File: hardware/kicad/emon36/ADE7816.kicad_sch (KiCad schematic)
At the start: 43 parts, among them J15 6_port_3.5mm_audio_jack_array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, J16 6_port_3.5mm_audio_jack_array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, U10 ADE7816

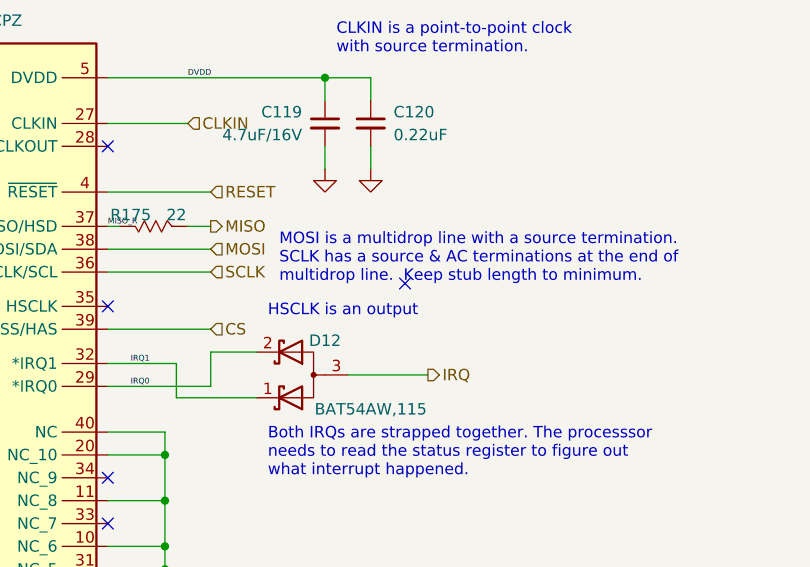
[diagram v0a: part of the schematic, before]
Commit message: Added diodes on IRQ, included solder mask and silk constraints, fix silk. Version sent to production.
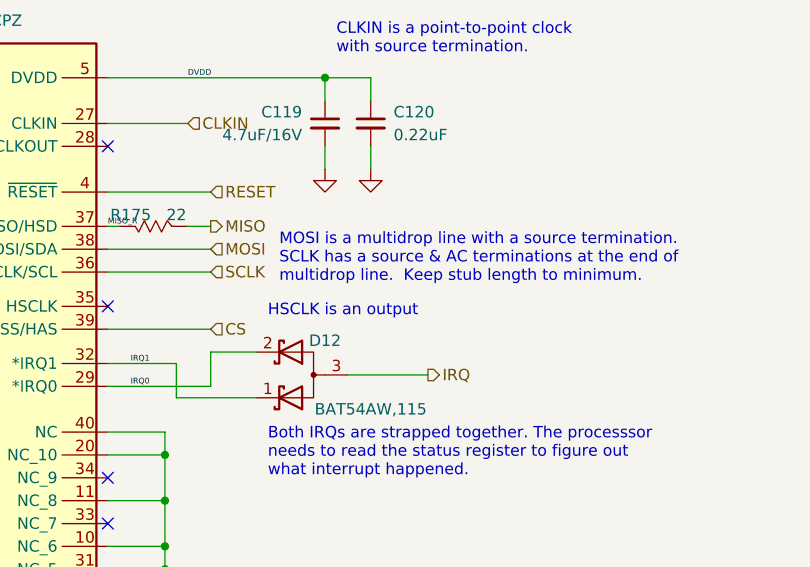
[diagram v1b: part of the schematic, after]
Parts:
- C107, C108, C109, C110, C111, C112, C117, C118: Desc (none) -> CAP CER 0.022UF 25V X7R 0603; MFR (none) -> Samsung Electro-Mechanics; MPN (none) -> CL10B222KB8NFNC
- C115, C120: Desc (none) -> CAP CER 0.22UF 25V X7R 0603; MFR (none) -> Samsung Electro-Mechanics; MPN (none) -> CL10B224KA8NNNC
- C116: Desc (none) -> CAP CER 0.1UF 50V X7R 0603; MFR (none) -> KYOCERA AVX; MPN (none) -> 06035C104KAT2A
- D12: Desc (none) -> DIODE ARRAY SCHOTTKY 30V SOT323
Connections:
- no-connect marks 19 -> 18
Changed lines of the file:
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@@
   (no_connect (at 46.99 53.34))
   (no_connect (at 195.58 62.23))
-  (no_connect (at 228.6 77.47))
   (no_connect (at 195.58 80.01))
   (wire (pts (xy 160.02 68.58) (xy 148.59 68.58))
@@
       (effects (font (size 1.27 1.27)) hide)
     )
+    (property "Desc" "CAP CER 0.022UF 25V X7R 0603" (id 4) (at 85.09 106.68 0)
+      (effects (font (size 1.27 1.27)) hide)
+    )
+    (property "MFR" "Samsung Electro-Mechanics" (id 5) (at 85.09 106.68 0)
+      (effects (font (size 1.27 1.27)) hide)
+    )
+    (property "MPN" "CL10B222KB8NFNC" (id 6) (at 85.09 106.68 0)
+      (effects (font (size 1.27 1.27)) hide)
+    )
     (pin "1")
     (pin "2")
@@
       (effects (font (size 1.27 1.27)) hide)
     )
+    (property "Desc" "CAP CER 0.022UF 25V X7R 0603" (id 4) (at 85.09 54.61 0)
+      (effects (font (size 1.27 1.27)) hide)
+    )
+    (property "MFR" "Samsung Electro-Mechanics" (id 5) (at 85.09 54.61 0)
+      (effects (font (size 1.27 1.27)) hide)
+    )
+    (property "MPN" "CL10B222KB8NFNC" (id 6) (at 85.09 54.61 0)
+      (effects (font (size 1.27 1.27)) hide)
+    )
     (pin "1")
     (pin "2")
@@
     )
     (property "MPN" "BAT54AW,115" (id 5) (at 224.79 91.44 0))
+    (property "Desc" "DIODE ARRAY SCHOTTKY 30V SOT323" (id 6) (at 217.17 87.63 0)
+      (effects (font (size 1.27 1.27)) hide)
+    )
     (pin "1")
     (pin "2")
@@
     )
     (property "Datasheet" "~" (id 3) (at 143.51 78.74 0)
+      (effects (font (size 1.27 1.27)) hide)
+    )
+    (property "Desc" "CAP CER 0.1UF 50V X7R 0603" (id 4) (at 143.51 78.74 0)
+      (effects (font (size 1.27 1.27)) hide)
+    )
+    (property "MFR" "KYOCERA AVX" (id 5) (at 143.51 78.74 0)
+      (effects (font (size 1.27 1.27)) hide)
+    )
+    (property "MPN" "06035C104KAT2A" (id 6) (at 143.51 78.74 0)
       (effects (font (size 1.27 1.27)) hide)
     )
@@
       (effects (font (size 1.27 1.27)) hide)
     )
+    (property "Desc" "CAP CER 0.22UF 25V X7R 0603" (id 4) (at 143.51 63.5 0)
+      (effects (font (size 1.27 1.27)) hide)
+    )
+    (property "MFR" "Samsung Electro-Mechanics" (id 5) (at 143.51 63.5 0)
+      (effects (font (size 1.27 1.27)) hide)
+    )
+    (property "MPN" "CL10B224KA8NNNC" (id 6) (at 143.51 63.5 0)
+      (effects (font (size 1.27 1.27)) hide)
+    )
     (pin "1")
     (pin "2")
@@
       (effects (font (size 1.27 1.27)) hide)
     )
+    (property "Desc" "CAP CER 0.022UF 25V X7R 0603" (id 4) (at 143.51 99.06 0)
+      (effects (font (size 1.27 1.27)) hide)
+    )
+    (property "MFR" "Samsung Electro-Mechanics" (id 5) (at 143.51 99.06 0)
+      (effects (font (size 1.27 1.27)) hide)
+    )
+    (property "MPN" "CL10B222KB8NFNC" (id 6) (at 143.51 99.06 0)
+      (effects (font (size 1.27 1.27)) hide)
+    )
     (pin "1")
     (pin "2")
@@
       (effects (font (size 1.27 1.27)) hide)
     )
+    (property "Desc" "CAP CER 0.22UF 25V X7R 0603" (id 4) (at 224.79 59.69 0)
+      (effects (font (size 1.27 1.27)) hide)
+    )
+    (property "MFR" "Samsung Electro-Mechanics" (id 5) (at 224.79 59.69 0)
+      (effects (font (size 1.27 1.27)) hide)
+    )
+    (property "MPN" "CL10B224KA8NNNC" (id 6) (at 224.79 59.69 0)
+      (effects (font (size 1.27 1.27)) hide)
+    )
     (pin "1")
     (pin "2")
@@
     )
     (property "Datasheet" "~" (id 3) (at 143.51 115.57 0)
+      (effects (font (size 1.27 1.27)) hide)
+    )
+    (property "Desc" "CAP CER 0.022UF 25V X7R 0603" (id 4) (at 143.51 115.57 0)
+      (effects (font (size 1.27 1.27)) hide)
+    )
+    (property "MFR" "Samsung Electro-Mechanics" (id 5) (at 143.51 115.57 0)
+      (effects (font (size 1.27 1.27)) hide)
+    )
+    (property "MPN" "CL10B222KB8NFNC" (id 6) (at 143.51 115.57 0)
       (effects (font (size 1.27 1.27)) hide)
     )
@@
       (effects (font (size 1.27 1.27)) hide)
     )
+    (property "Desc" "CAP CER 0.022UF 25V X7R 0603" (id 4) (at 85.09 121.92 0)
+      (effects (font (size 1.27 1.27)) hide)
+    )
+    (property "MFR" "Samsung Electro-Mechanics" (id 5) (at 85.09 121.92 0)
+      (effects (font (size 1.27 1.27)) hide)
+    )
+    (property "MPN" "CL10B222KB8NFNC" (id 6) (at 85.09 121.92 0)
+      (effects (font (size 1.27 1.27)) hide)
+    )
     (pin "1")
     (pin "2")
@@
     )
     (property "Datasheet" "~" (id 3) (at 85.09 69.85 0)
+      (effects (font (size 1.27 1.27)) hide)
+    )
+    (property "Desc" "CAP CER 0.022UF 25V X7R 0603" (id 4) (at 85.09 69.85 0)
+      (effects (font (size 1.27 1.27)) hide)
+    )
+    (property "MFR" "Samsung Electro-Mechanics" (id 5) (at 85.09 69.85 0)
+      (effects (font (size 1.27 1.27)) hide)
+    )
+    (property "MPN" "CL10B222KB8NFNC" (id 6) (at 85.09 69.85 0)
       (effects (font (size 1.27 1.27)) hide)
     )
@@
       (effects (font (size 1.27 1.27)) hide)
     )
+    (property "Desc" "CAP CER 0.022UF 25V X7R 0603" (id 4) (at 85.09 85.09 0)
+      (effects (font (size 1.27 1.27)) hide)
+    )
+    (property "MFR" "Samsung Electro-Mechanics" (id 5) (at 85.09 85.09 0)
+      (effects (font (size 1.27 1.27)) hide)
+    )
+    (property "MPN" "CL10B222KB8NFNC" (id 6) (at 85.09 85.09 0)
+      (effects (font (size 1.27 1.27)) hide)
+    )
     (pin "1")
     (pin "2")
@@
       (effects (font (size 1.27 1.27)) hide)
     )
+    (property "Desc" "CAP CER 0.022UF 25V X7R 0603" (id 4) (at 85.09 137.16 0)
+      (effects (font (size 1.27 1.27)) hide)
+    )
+    (property "MFR" "Samsung Electro-Mechanics" (id 5) (at 85.09 137.16 0)
+      (effects (font (size 1.27 1.27)) hide)
+    )
+    (property "MPN" "CL10B222KB8NFNC" (id 6) (at 85.09 137.16 0)
+      (effects (font (size 1.27 1.27)) hide)
+    )
